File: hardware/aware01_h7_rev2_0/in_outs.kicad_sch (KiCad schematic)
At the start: 28 parts, among them J3 InL, J4 InR, J5 OutL, J6 OutR, U10 NE5532DRG4, U11 NE5532DRG4

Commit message: hw: improve layout, update BOM
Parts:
- C54, C55: Manufacturer_Name (none) -> KYOCERA AVX; Manufacturer_Part_Number (none) -> KGM15ACG1E180JT; Mouser Part Number (none) -> 581-KGM15ACG1E180JT
- D4, D5: Manufacturer_Name (none) -> Vishay Semiconductors; Manufacturer_Part_Number (none) -> BAT54C-E3-08; Mouser Part Number (none) -> 78-BAT54C-E3-08
- R14, R15: Manufacturer_Name (none) -> YAGEO; Manufacturer_Part_Number (none) -> RC0603JR-1012KL; Mouser Part Number (none) -> 603-RC0603JR-1012KL
- R16, R17: Manufacturer_Name (none) -> YAGEO; Manufacturer_Part_Number (none) -> RC0603JR-071K8L; Mouser Part Number (none) -> 603-RC0603JR-071K8L
- R18, R19: Manufacturer_Name (none) -> YAGEO; Manufacturer_Part_Number (none) -> RC0603FR-105K6L; Mouser Part Number (none) -> 603-RC0603FR-105K6L
- R20, R21: Manufacturer_Name (none) -> YAGEO; Manufacturer_Part_Number (none) -> RE0603BRE0739KL; Mouser Part Number (none) -> 603-RE0603BRE0739KL
- R22, R23: Manufacturer_Name (none) -> YAGEO; Manufacturer_Part_Number (none) -> RT0603FRE071KL; Mouser Part Number (none) -> 603-RT0603FRE071KL

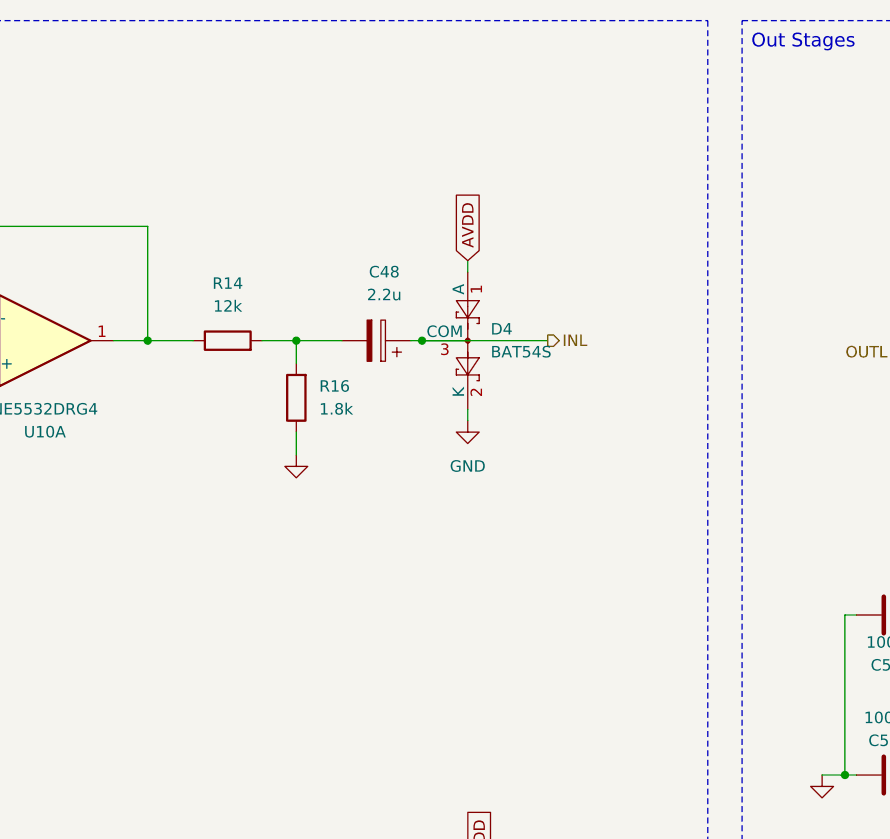
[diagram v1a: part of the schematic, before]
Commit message: hw: update tactile switch footprints and BOM entry
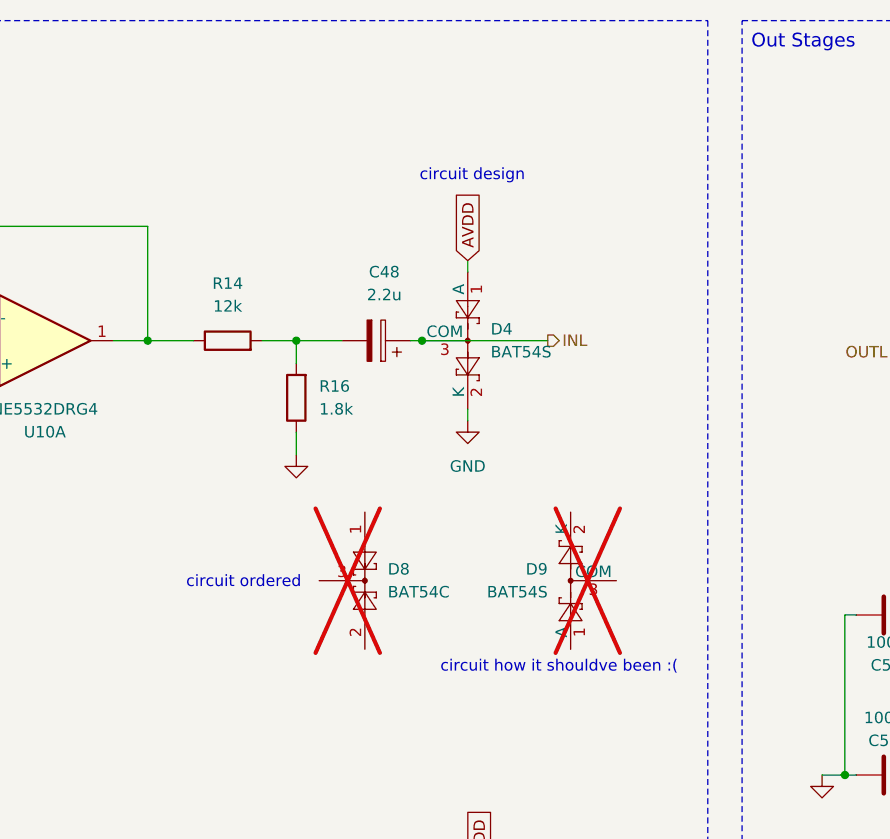
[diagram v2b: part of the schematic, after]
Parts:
- added D8: BAT54C, Package_TO_SOT_SMD:SOT-23, symbol Diode:BAT54C
- added D9: BAT54S, Package_TO_SOT_SMD:SOT-23, symbol Diode:BAT54S
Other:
- note added: "circuit design"
- note added: "circuit how it shouldve been :("
- note added: "circuit ordered"
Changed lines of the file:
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@@
+		)
+	)
+	(text "circuit design"
+		(exclude_from_sim no)
+		(at 119.888 46.482 0)
+		(effects
+			(font
+				(size 1.27 1.27)
+			)
+		)
+	)
+	(text "circuit how it shouldve been :("
+		(exclude_from_sim no)
+		(at 129.54 101.092 0)
+		(effects
+			(font
+				(size 1.27 1.27)
+			)
 		)
 	)
@@
 			)
 			(justify left top)
+		)
+	)
+	(text "circuit ordered"
+		(exclude_from_sim no)
+		(at 94.488 91.694 0)
+		(effects
+			(font
+				(size 1.27 1.27)
+			)
 		)
 	)
@@
 					(unit 1)
 				)
+			)
+		)
+	)
+	(symbol
+		(lib_id "Diode:BAT54C")
+		(at 107.95 91.44 270)
+		(unit 1)
+		(exclude_from_sim no)
+		(in_bom no)
+		(on_board no)
+		(dnp yes)
+		(fields_autoplaced yes)
+		(property "Reference" "D8"
+			(at 110.49 90.1699 90)
+			(effects
+				(font
+					(size 1.27 1.27)
+				)
+				(justify left)
+			)
+		)
+		(property "Value" "BAT54C"
+			(at 110.49 92.7099 90)
+			(effects
+				(font
+					(size 1.27 1.27)
+				)
+				(justify left)
+			)
+		)
+		(property "Footprint" "Package_TO_SOT_SMD:SOT-23"
+			(at 111.125 93.345 0)
+			(effects
+				(font
+					(size 1.27 1.27)
+				)
+				(justify left)
+				(hide yes)
+			)
+		)
+		(property "Datasheet" "http://www.diodes.com/_files/datasheets/ds11005.pdf"
+			(at 107.95 89.408 0)
+			(effects
+				(font
+					(size 1.27 1.27)
+				)
+				(hide yes)
+			)
+		)
+		(property "Description" "dual schottky barrier diode, common cathode"
+			(at 107.95 91.44 0)
+			(effects
+				(font
+					(size 1.27 1.27)
+				)
+				(hide yes)
+			)
+		)
+		(pin "3"
+		)
+		(pin "1"
+		)
+		(pin "2"
+		)
+		(instances
+			(project ""
+				(path "/efd43d7c-3c18-45dd-8fa5-4bf32165850f/50dd69da-5058-483c-924f-252f04b072bd/9f63702e-8ad6-4a2d-8a3d-8a8b3f17f2a4"
+					(reference "D8")
+					(unit 1)
+				)
+			)
+		)
+	)
+	(symbol
+		(lib_id "Diode:BAT54S")
+		(at 130.81 91.44 90)
+		(unit 1)
+		(exclude_from_sim no)
+		(in_bom no)
+		(on_board no)
+		(dnp yes)
+		(fields_autoplaced yes)
+		(property "Reference" "D9"
+			(at 128.27 90.1699 90)
+			(effects
+				(font
+					(size 1.27 1.27)
+				)
+				(justify left)
+			)
+		)
+		(property "Value" "BAT54S"
+			(at 128.27 92.7099 90)
+			(effects
+				(font
+					(size 1.27 1.27)
+				)
+				(justify left)
+			)
+		)
+		(property "Footprint" "Package_TO_SOT_SMD:SOT-23"
+			(at 127.635 89.535 0)
+			(effects
+				(font
+					(size 1.27 1.27)
+				)
+				(justify left)
+				(hide yes)
+			)
+		)
+		(property "Datasheet" "https://www.diodes.com/assets/Datasheets/ds11005.pdf"
+			(at 130.81 94.488 0)
+			(effects
+				(font
+					(size 1.27 1.27)
+				)
+				(hide yes)
+			)
+		)
+		(property "Description" "Vr 30V, If 200mA, Dual schottky barrier diode, in series, SOT-323"
+			(at 130.81 91.44 0)
+			(effects
+				(font
+					(size 1.27 1.27)
+				)
+				(hide yes)
+			)
+		)
+		(pin "2"
+		)
+		(pin "3"
+		)
+		(pin "1"
+		)
+		(instances
+			(project ""
+				(path "/efd43d7c-3c18-45dd-8fa5-4bf32165850f/50dd69da-5058-483c-924f-252f04b072bd/9f63702e-8ad6-4a2d-8a3d-8a8b3f17f2a4"
+					(reference "D9")
+					(unit 1)
+				)

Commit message: hw: update schematic
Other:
- company: Ausschussware -> Aware Modular

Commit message: update hardware repo
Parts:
- removed D8: BAT54C, Package_TO_SOT_SMD:SOT-23, symbol Diode:BAT54C
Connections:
- net AVDD: now also D9.2 (K)
- net GND: now also D9.1 (A)
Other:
- note added: "Circuit how it shouldve been. Adjusted in revision 3"
- note removed: "circuit how it shouldve been :("
- note removed: "circuit ordered"
- title: Aware 01 - Eurorack DSP Module -> Aarebot - Eurorack DSP Module
- moved on the sheet: C46, C47, C49, C50, C51, D5, D9, R16, U10C, U11C
